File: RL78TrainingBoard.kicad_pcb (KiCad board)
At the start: 2 copper layers, 0 parts

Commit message: フットプリント作成
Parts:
- added ?: , , F.Cu at (186.6, 142.8)
- added C1: 0.1uF, RL78TrainingBoard:1608Metric, F.Cu at (135.0, 145.0)
- added C10: 0.1uF, RL78TrainingBoard:1608Metric, F.Cu at (182.7, 101.5)
- added C11: 0.1uF, RL78TrainingBoard:1608Metric, F.Cu at (153.0, 127.6)
- added C12: 10pF, RL78TrainingBoard:1005Metric, F.Cu at (103.1, 148.7)
- added C13: 0.1uF, RL78TrainingBoard:1608Metric, F.Cu at (168.8, 114.0)
- added C14: 1uF, RL78TrainingBoard:1608Metric, F.Cu at (136.2, 139.8)
- added C15: 0.1uF, RL78TrainingBoard:1608Metric, F.Cu at (140.6, 139.8)
- added C16: 0.1uF, RL78TrainingBoard:1608Metric, F.Cu at (188.1, 93.8)
- added C17: 100uF, RL78TrainingBoard:3216Metric, F.Cu at (203.1, 72.1)
- added C18: 0.1uF, RL78TrainingBoard:1608Metric, F.Cu at (145.0, 137.2)
- added C19: 0.1uF, RL78TrainingBoard:1608Metric, F.Cu at (149.4, 132.8)
- added C2: 39pF, RL78TrainingBoard:1608Metric, F.Cu at (151.3, 130.2)
- added C20: 1uF, RL78TrainingBoard:1608Metric, F.Cu at (140.6, 137.2)
- added C21: 1uF, RL78TrainingBoard:1608Metric, F.Cu at (124.8, 148.0)
- added C3: 39pF, RL78TrainingBoard:1608Metric, F.Cu at (202.3, 77.7)
- added C4: 100uF, RL78TrainingBoard:CP_Elec_6.3x7.7, F.Cu at (205.2, 66.4)
- added C5: 0.1uF, RL78TrainingBoard:1608Metric, F.Cu at (202.3, 75.1)
- added C6: 0.1uF, RL78TrainingBoard:1608Metric, F.Cu at (146.9, 130.2)
- added C7: 0.1uF, RL78TrainingBoard:1608Metric, F.Cu at (191.3, 83.7)
- added C8: 0.1uF, RL78TrainingBoard:1608Metric, F.Cu at (133.7, 147.9)
- added C9: 10pF, RL78TrainingBoard:1005Metric, F.Cu at (106.2, 148.7)
- added D1: BYTE_LED, RL78TrainingBoard:1608Metric, F.Cu at (142.5, 132.0)
- added D10: USER_LED, RL78TrainingBoard:1608Metric, F.Cu at (156.5, 122.6)
- added D2: BYTE_LED, RL78TrainingBoard:1608Metric, F.Cu at (202.3, 80.3)
- added D3: BYTE_LED, RL78TrainingBoard:1608Metric, F.Cu at (217.1, 63.6)
- added D4: BYTE_LED, RL78TrainingBoard:1608Metric, F.Cu at (212.7, 66.2)
- added D5: BYTE_LED, RL78TrainingBoard:1608Metric, F.Cu at (197.8, 80.1)
- added D6: BYTE_LED, RL78TrainingBoard:1608Metric, F.Cu at (135.6, 142.4)
- added D7: BYTE_LED, RL78TrainingBoard:1608Metric, F.Cu at (164.3, 111.4)
- added D8: BYTE_LED, RL78TrainingBoard:1608Metric, F.Cu at (195.7, 83.7)
- added D9: POWER, RL78TrainingBoard:1608Metric, F.Cu at (165.3, 116.7)
- added F1: Polyfuse, RL78TrainingBoard:3216Metric, F.Cu at (130.3, 141.4)
- added J1: USB_B_Mini, RL78TrainingBoard:UX60SC-MB-5ST, F.Cu at (85.2, 147.3)
- added J2: DSub9pin_Male, RL78TrainingBoard:DSUB-9_Male_Horizontal_P2.77x2.84mm_EdgePinOffset7.70mm_Housed_MountingHolesOffset9.12mm, F.Cu at (164.9, 65.6)
- added J3: Debugger, RL78TrainingBoard:IDC-Header_2x07_P2.54mm_Vertical, F.Cu at (119.0, 107.2)
- added J4: OLED, RL78TrainingBoard:OLED, F.Cu at (167.2, 96.8)
- added JP1: UART_TXD_Jumper, RL78TrainingBoard:Jumper_1x03_P2.54mm, F.Cu at (144.0, 120.7)
- added JP2: UART_RXD_Jumper, RL78TrainingBoard:Jumper_1x03_P2.54mm, F.Cu at (124.9, 139.4)
- added L1: L, RL78TrainingBoard:1608Metric, F.Cu at (142.5, 129.3)
- added LS1: Buzzer, RL78TrainingBoard:PKMCS0909E4000-R1, F.Cu at (73.7, 144.2)
- added LS2: Speaker, RL78TrainingBoard:UM1515IA085008, F.Cu at (122.3, 129.0)
- added Q1: AO3400A, RL78TrainingBoard:SOT-23, F.Cu at (140.0, 143.3)
- added Q2: NJL7502L, RL78TrainingBoard:NJL7502L, F.Cu at (181.9, 92.4)
- added R1: 1k, RL78TrainingBoard:1608Metric, F.Cu at (212.7, 68.8)
- added R10: 1k, RL78TrainingBoard:1608Metric, F.Cu at (191.3, 86.3)
- added R11: 27, RL78TrainingBoard:1608Metric, F.Cu at (156.5, 120.0)
- added R12: 27, RL78TrainingBoard:1608Metric, F.Cu at (168.8, 111.4)
- added R13: 10k, RL78TrainingBoard:1608Metric, F.Cu at (164.3, 114.0)
- added R14: 10k, RL78TrainingBoard:1608Metric, F.Cu at (208.3, 71.8)
- added R15: 10k, RL78TrainingBoard:1608Metric, F.Cu at (197.8, 77.5)
- added R16: 1k, RL78TrainingBoard:1608Metric, F.Cu at (136.2, 137.1)
- added R17: 10k, RL78TrainingBoard:1608Metric, F.Cu at (206.7, 77.7)
- added R18: 100, RL78TrainingBoard:1608Metric, F.Cu at (145.0, 134.6)
- added R19: 10k, RL78TrainingBoard:1608Metric, F.Cu at (182.7, 96.2)
- added R2: 1k, RL78TrainingBoard:1608Metric, F.Cu at (129.2, 148.0)
- added R20: 100, RL78TrainingBoard:1608Metric, F.Cu at (160.9, 117.8)
- added R21: 2.2k, RL78TrainingBoard:1608Metric, F.Cu at (212.7, 71.5)
- added R22: 2.2k, RL78TrainingBoard:1608Metric, F.Cu at (148.6, 127.6)
- added R23: 10k, RL78TrainingBoard:1608Metric, F.Cu at (140.6, 134.6)
- added R24: 10k, RL78TrainingBoard:1608Metric, F.Cu at (160.9, 123.0)
- added R25: 1k, RL78TrainingBoard:1608Metric, F.Cu at (126.7, 119.0)
- added R3: 1k, RL78TrainingBoard:1608Metric, F.Cu at (182.7, 98.8)
- added R4: 1k, RL78TrainingBoard:1608Metric, F.Cu at (160.9, 120.4)
- added R5: 1k, RL78TrainingBoard:1608Metric, F.Cu at (188.1, 91.1)
- added R6: 1k, RL78TrainingBoard:1608Metric, F.Cu at (206.7, 75.1)
- added R7: 1k, RL78TrainingBoard:1608Metric, F.Cu at (195.7, 86.3)
- added R8: 1k, RL78TrainingBoard:1608Metric, F.Cu at (212.7, 63.6)
- added R9: 2.2k, RL78TrainingBoard:1608Metric, F.Cu at (187.1, 96.4)
- added REF**: Hole, RL78TrainingBoard:Hole, F.Cu at (174.6, 130.8)
- added RV1: 10k, RL78TrainingBoard:RV, F.Cu at (180.6, 128.2)
- added RV2: 10k, RL78TrainingBoard:RV, F.Cu at (189.2, 136.8)
- added RV3: 10k, RL78TrainingBoard:TSR-3323S, F.Cu at (150.3, 119.5)
- added RV4: 10k, RL78TrainingBoard:TSR-3386K, F.Cu at (96.2, 142.7)
- added RV5: 10k, RL78TrainingBoard:Volume_RK10J, F.Cu at (144.1, 101.0)
- added SW1: SW_A, RL78TrainingBoard:SW_PUSH_6mm, F.Cu at (133.2, 120.4)
- added SW2: SW_B, RL78TrainingBoard:SW_PUSH_6mm, F.Cu at (149.1, 112.1)
- added SW3: SW_C, RL78TrainingBoard:SW_PUSH_6mm, F.Cu at (103.5, 141.1)
- added SW4: SW_D, RL78TrainingBoard:SW_PUSH_6mm, F.Cu at (114.1, 141.1)
- added SW5: RESET_SW, RL78TrainingBoard:SW_TVAF06, F.Cu at (159.9, 113.3)
- added SW6: USER_SW, RL78TrainingBoard:SW_PUSH_6mm, F.Cu at (138.5, 111.8)
- added U1: TBD62783A, RL78TrainingBoard:SOP-18_7x12.5mm_P1.27mm, F.Cu at (193.8, 69.2)
- added U2: FT230XS, RL78TrainingBoard:SSOP-16_3.9x4.9mm_P0.635mm, F.Cu at (191.6, 79.3)
- added U3: ADM3202, RL78TrainingBoard:TSSOP-16-1EP_4.4x5mm_P0.65mm, F.Cu at (136.1, 130.0)
- added U4: SC1602B, RL78TrainingBoard:SC1602, F.Cu at (70.4, 77.9)
- added U5: RL78G13_64pin, RL78TrainingBoard:LQFP-64-12x12mm-P0.65mm_FusionPCB, F.Cu at (90.7, 116.3)
- added U6: LM60, RL78TrainingBoard:SOT-23, F.Cu at (217.0, 67.1)
- added U7: YMZ294, RL78TrainingBoard:DIP-18_W7.62mm_Socket, F.Cu at (127.0, 95.4)
- added U8: HT82V739, RL78TrainingBoard:SOP-8_3.9x4.9mm_P1.27mm, F.Cu at (185.1, 86.7)
- added Y1: 32.768kHz, RL78TrainingBoard:Crystal_SMD_3215-2Pin, F.Cu at (130.0, 144.8)
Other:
- board outline added: 100 x 100 mm

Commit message: 基板設計(部品仮配置)
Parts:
- moved C3 248.6 mm to (-29.1, -13.0), turned to 180 degrees
- moved C5 247.5 mm to (-25.0, -23.0)
- moved R14 245.7 mm to (-21.0, -16.5)
- moved C4 245.7 mm to (-21.0, -29.5)
- moved R8 242.7 mm to (-15.8, -18.5)
- moved R9 241.7 mm to (-35.1, 1.50)
- moved ? 240.9 mm to (-34.0, 46.0)
- moved REF** 240.9 mm to (-46.0, 34.0)
- moved RV2 240.9 mm to (-31.4, 40.0)
- moved RV1 240.9 mm to (-40.0, 31.4)
- moved U2 240.9 mm to (-28.5, -18.5)
- moved R15 239.8 mm to (-21.0, -20.5)
- moved RV3 239.6 mm to (-21.0, -48.0)
- moved R10 238.3 mm to (-32.0, 3.00)
- moved C7 236.9 mm to (-12.5, -37.0)
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
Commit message: 部品見直し
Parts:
- removed JP1: UART_TXD_Jumper, RL78TrainingBoard:Jumper_1x03_P2.54mm
- removed JP2: UART_RXD_Jumper, RL78TrainingBoard:Jumper_1x03_P2.54mm
- added REF**: TestPoint_THTPad_Drill0.9mm, RL78TrainingBoard:TestPoint_THTPad_Drill0.9mm, F.Cu at (-25.0, 43.0)
- added REF**: TestPoint_THTPad_Drill0.9mm, RL78TrainingBoard:TestPoint_THTPad_Drill0.9mm, F.Cu at (23.0, 43.0)
- added SW7: SW_SPDT, RL78TrainingBoard:2MS1-T2-B4-M2-Q-E-S, F.Cu at (-35.4, -3.70)
- added SW8: SW_DPDT_x2, RL78TrainingBoard:IS-2235-G, F.Cu at (-43.5, -14.2)
- moved D9 4.00 mm to (-35.1, 1.00)
- moved R9 2.50 mm to (-35.1, 4.00)
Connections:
- J1 pad 1: Net-(F1-Pad2) -> VBUS
- J3 pad 8: +5V -> VBUS
- J3 pad 9: +5V -> VBUS
- L1 pad 1: +5V -> Net-(F1-Pad2)
- L1 pad 2: Net-(F1-Pad1) -> +5V

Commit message: 基板設計(部品配置)
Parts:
- moved R21 29.2 mm to (-21.0, 27.1), turned to 0 degrees
- moved R22 28.9 mm to (-21.0, 25.5), turned to 0 degrees
- moved C20 24.9 mm to (24.7, 25.0)
- moved R25 16.2 mm to (35.0, -22.0), turned to 90 degrees
- moved R8 13.9 mm to (-2.70, -23.4), turned to 90 degrees
- moved C13 13.4 mm to (-10.0, -40.0), turned to 180 degrees
- moved C1 13.1 mm to (20.0, -39.5), turned to 180 degrees
- moved C11 12.3 mm to (-10.0, -33.6), turned to 180 degrees
- moved C10 12.1 mm to (-10.0, -38.4)
- moved U2 11.9 mm to (-18.0, -24.0)
- moved R7 11.3 mm to (-1.10, -23.4), turned to 90 degrees
- moved R23 10.9 mm to (33.4, -22.0), turned to 90 degrees
- moved C19 10.8 mm to (23.1, 25.0)
- moved R14 10.8 mm to (-25.0, -26.5)
- moved R11 9.30 mm to (-25.0, -20.0)
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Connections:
- REF** pad : (no net) -> GND

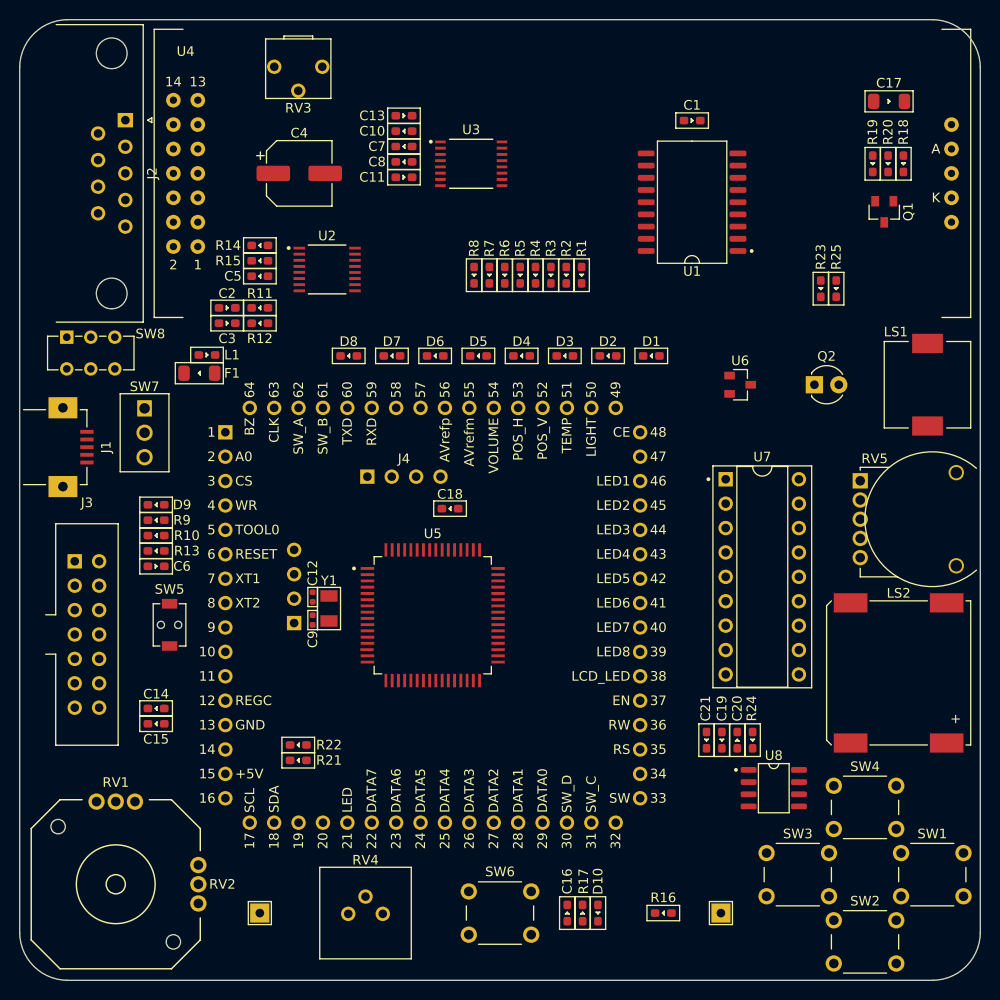
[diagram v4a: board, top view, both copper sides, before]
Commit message: 配線作成
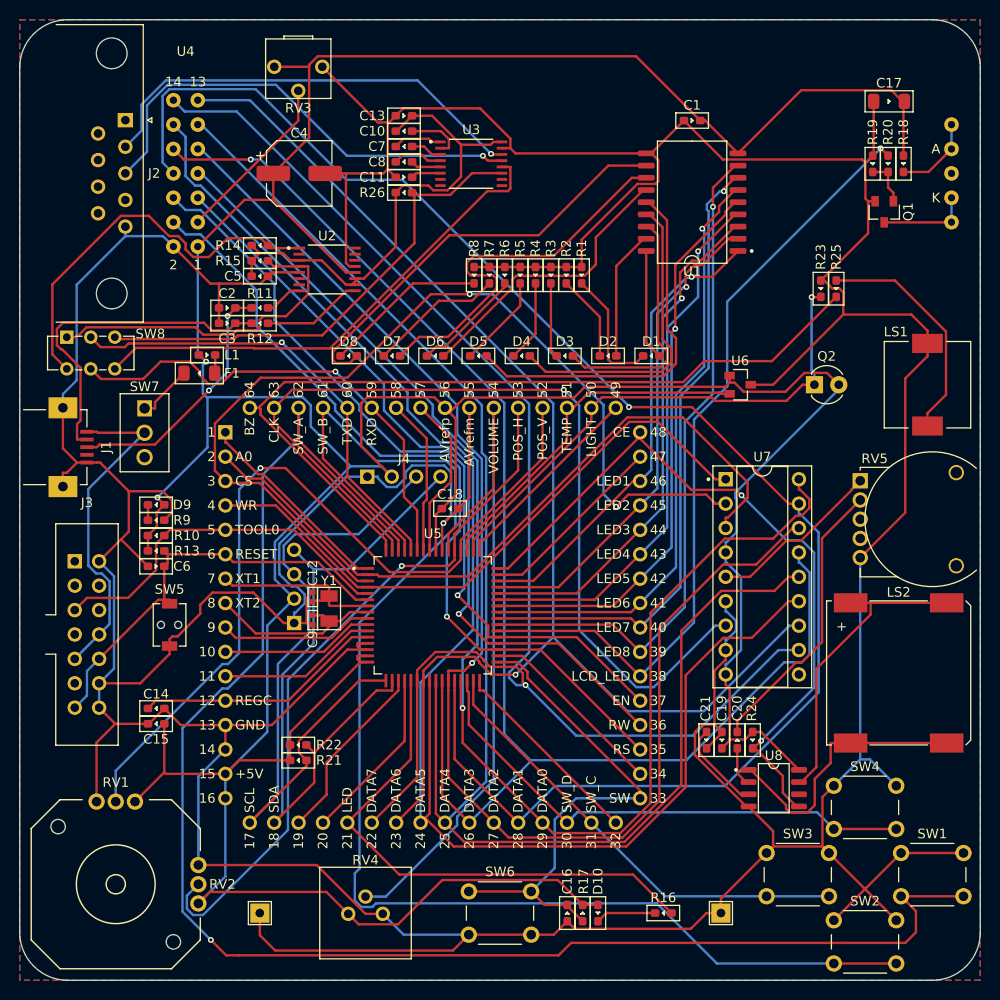
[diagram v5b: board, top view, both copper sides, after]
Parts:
- added R26: 10k, RL78TrainingBoard:1608Metric, F.Cu at (-10.0, -32.0)
- turned LS2 to -90 degrees
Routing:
- net GND: track 0.00 -> 636.6 mm, vias 0 -> 1
- net +5V: track 0.00 -> 448.5 mm, vias 0 -> 2
- net DATA1: track 0.00 -> 168.0 mm, vias 0 -> 1
- net SW_A: track 0.00 -> 167.0 mm, vias 0 -> 1
- net DATA5: track 0.00 -> 161.7 mm
- net DATA4: track 0.00 -> 160.8 mm
- net DATA3: track 0.00 -> 153.6 mm, vias 0 -> 1
- net DATA7: track 0.00 -> 147.8 mm, vias 0 -> 1
- net DATA0: track 0.00 -> 144.2 mm, vias 0 -> 1
- net SW_B: track 0.00 -> 143.3 mm
- net DATA2: track 0.00 -> 143.2 mm, vias 0 -> 1
- net DATA6: track 0.00 -> 140.5 mm, vias 0 -> 1
- net YMZ294_CS: track 0.00 -> 99.8 mm, vias 0 -> 2
- net YMZ294_CLK: track 0.00 -> 96.8 mm, vias 0 -> 1
- net POS_V: track 0.00 -> 86.5 mm, vias 0 -> 1
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- added copper zone on B.Cu, net GND
- added copper zone on F.Cu, net GND

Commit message: 基板 V1.0
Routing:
- net GND: vias 1 -> 61
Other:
- board text added: "BUZZER"
- board text added: "DSUB"
- board text added: "GND"
- board text added: "JOYSTICK"
- board text added: "LCD CONTRAST"
- board text added: "LED1"
- board text added: "LED2"
- board text added: "LED3"
- board text added: "LED4"
- board text added: "LED5"
- board text added: "LED6"
- board text added: "LED7"
- board text added: "LED8"
- board text added: "LIGHT"
- board text added: "OFF"
- board text added: "ON"
- board text added: "POEWR SW"
- board text added: "RESET SW"
- board text added: "RL78 G13"
- board text added: "RL78 Training Board V1.0"
- board text added: "SW A"
- board text added: "SW B"
- board text added: "SW C"
- board text added: "SW D"
- board text added: "TEMP"
- board text added: "UART SELECT"
- board text added: "USB"
- board text added: "USER LED"
- board text added: "USER SW"
- board text added: "USER VOLUME"
- board text added: "VOLUME"
